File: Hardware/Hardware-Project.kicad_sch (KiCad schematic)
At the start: 2 parts

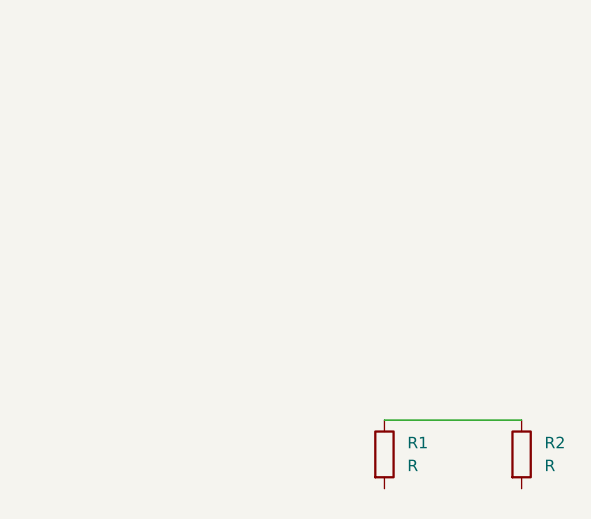
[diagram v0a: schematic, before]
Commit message: Added STM32F446RE symbol and footprint
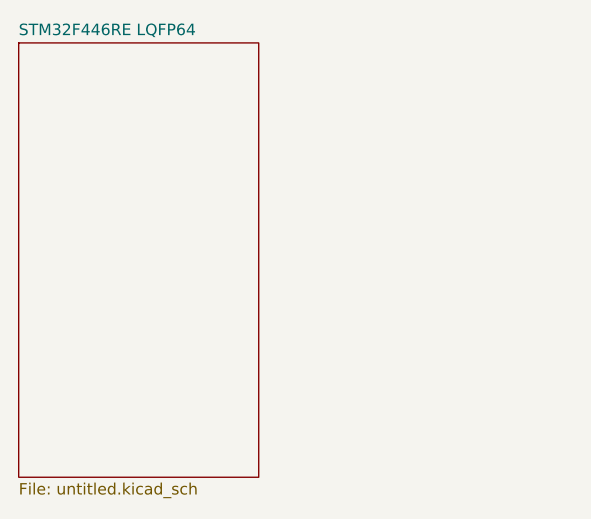
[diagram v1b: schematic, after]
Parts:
- removed R1, R2: R, symbol Device:R
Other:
- added sheet STM32F446RE LQFP64 (untitled.kicad_sch)
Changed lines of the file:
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@@
 	(generator_version "9.0")
 	(paper "A4")
-	(wire
-		(pts
-			(xy 91.44 80.01) (xy 106.68 80.01)
-		)
-		(stroke
-			(width 0)
-			(type default)
-		)
-	)
-	(symbol
-		(lib_id "Device:R")
-		(at 106.68 83.82 0)
-		(unit 1)
+	(sheet
+		(at 50.8 38.1)
+		(size 26.67 48.26)
 		(exclude_from_sim no)
 		(in_bom yes)
@@
 		(dnp no)
 		(fields_autoplaced yes)
-		(property "Reference" "R2"
-			(at 109.22 82.5499 0)
+		(stroke
+			(width 0.1524)
+			(type solid)
+		)
+		(fill
+			(color 0 0 0 0.0000)
+		)
+		(property "Sheetname" "STM32F446RE LQFP64"
+			(at 50.8 37.3884 0)
 			(effects
 				(font
 					(size 1.27 1.27)
 				)
-				(justify left)
+				(justify left bottom)
 			)
 		)
-		(property "Value" "R"
-			(at 109.22 85.0899 0)
+		(property "Sheetfile" "untitled.kicad_sch"
+			(at 50.8 86.9446 0)
 			(effects
 				(font
 					(size 1.27 1.27)
 				)
-				(justify left)
+				(justify left top)
 			)
-		)
-		(property "Footprint" ""
-			(at 104.902 83.82 90)
-			(effects
-				(font
-					(size 1.27 1.27)
-				)
-				(hide yes)
-			)
-		)
-		(property "Datasheet" "~"
-			(at 106.68 83.82 0)
-			(effects
-				(font
-					(size 1.27 1.27)
-				)
-				(hide yes)
-			)
-		)
-		(property "Description" "Resistor"
-			(at 106.68 83.82 0)
-			(effects
-				(font
-					(size 1.27 1.27)
-				)
-				(hide yes)
-			)
-		)
-		(pin "2"
-		)
-		(pin "1"
 		)
 		(instances
 			(project "Hardware-Project"
 				(path "/16e232dd-2018-4914-997b-dd1e00d4fd91"
-					(reference "R2")
-					(unit 1)
+					(page "2")
 				)
 			)
-		)
-	)
-	(symbol
-		(lib_id "Device:R")
-		(at 91.44 83.82 0)
-		(unit 1)
-		(exclude_from_sim no)
-		(in_bom yes)
-		(on_board yes)
-		(dnp no)
-		(fields_autoplaced yes)
-		(property "Reference" "R1"
-			(at 93.98 82.5499 0)
-			(effects
-				(font
-					(size 1.27 1.27)
-				)
-				(justify left)
-			)
-		)
-		(property "Value" "R"
-			(at 93.98 85.0899 0)
-			(effects
-				(font
-					(size 1.27 1.27)
-				)
-				(justify left)
-			)
-		)
-		(property "Footprint" ""
-			(at 89.662 83.82 90)
-			(effects
-				(font
-					(size 1.27 1.27)
-				)
-				(hide yes)
-			)
-		)
-		(property "Datasheet" "~"
-			(at 91.44 83.82 0)
-			(effects
-				(font
-					(size 1.27 1.27)
-				)
-				(hide yes)
-			)
-		)
-		(property "Description" "Resistor"
-			(at 91.44 83.82 0)
-			(effects
-				(font
-					(size 1.27 1.27)
-				)
-				(hide yes)
-			)
-		)
-		(pin "2"
-		)
-		(pin "1"
-		)
-		(instances
-			(project ""
-				(path "/16e232dd-2018-4914-997b-dd1e00d4fd91"
-					(reference "R1")
-					(unit 1)
-				)
-			)

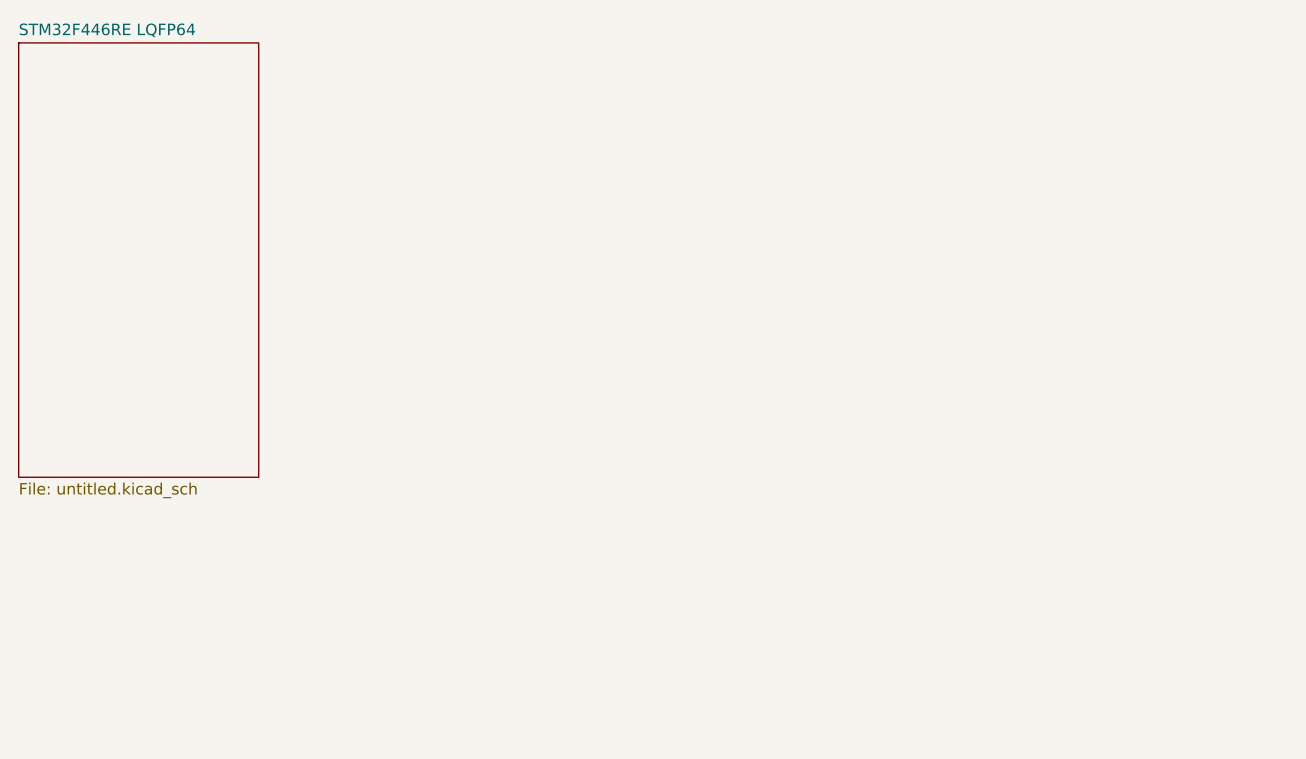
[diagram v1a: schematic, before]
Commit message: Added hierarchal sheets for the IMU and USB connectors. FInalized the design of USB and ESD protection
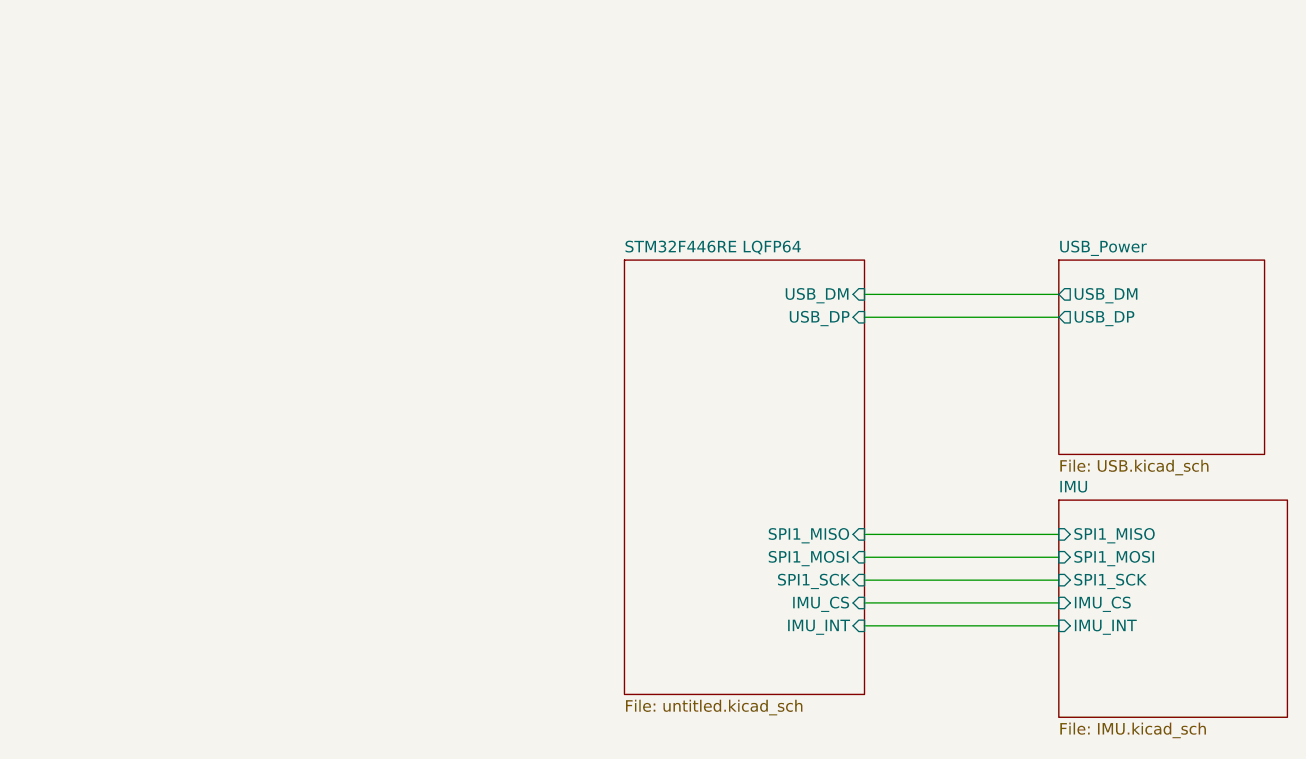
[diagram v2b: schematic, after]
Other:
- added sheet IMU (IMU.kicad_sch)
- added sheet USB_Power (USB.kicad_sch)
- sheet STM32F446RE LQFP64 ports: added IMU_CS, IMU_INT, SPI1_MISO, SPI1_MOSI, SPI1_SCK, USB_DM, USB_DP; removed none

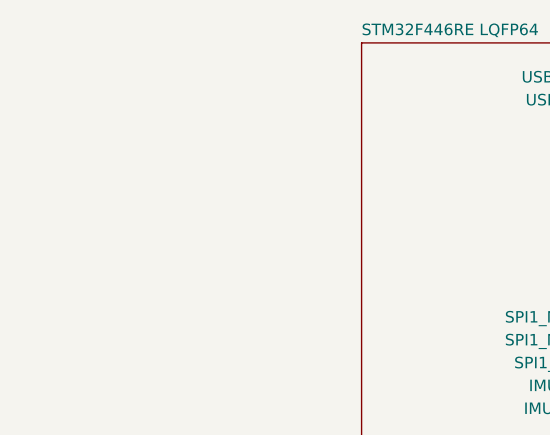
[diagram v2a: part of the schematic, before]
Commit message: Added the SD Card reader component.
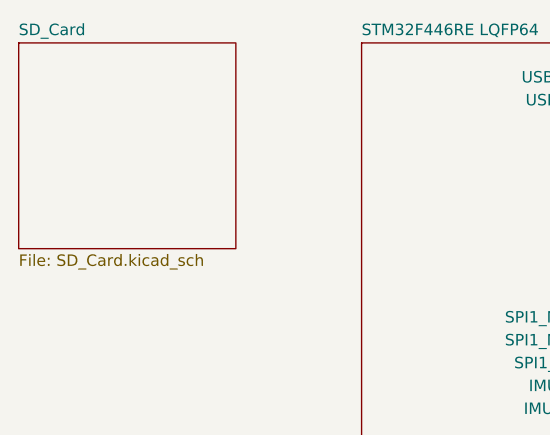
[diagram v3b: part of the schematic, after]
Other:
- added sheet SD_Card (SD_Card.kicad_sch)
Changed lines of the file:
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@@
+	)
+	(sheet
+		(at 80.01 62.23)
+		(size 24.13 22.86)
+		(exclude_from_sim no)
+		(in_bom yes)
+		(on_board yes)
+		(dnp no)
+		(fields_autoplaced yes)
+		(stroke
+			(width 0.1524)
+			(type solid)
+		)
+		(fill
+			(color 0 0 0 0.0000)
+		)
+		(property "Sheetname" "SD_Card"
+			(at 80.01 61.5184 0)
+			(effects
+				(font
+					(size 1.27 1.27)
+				)
+				(justify left bottom)
+			)
+		)
+		(property "Sheetfile" "SD_Card.kicad_sch"
+			(at 80.01 85.6746 0)
+			(effects
+				(font
+					(size 1.27 1.27)
+				)
+				(justify left top)
+			)
+		)
+		(instances
+			(project "Hardware-Project"
+				(path "/16e232dd-2018-4914-997b-dd1e00d4fd91"
+					(page "5")
+				)
+			)
+		)
 	)
 	(sheet

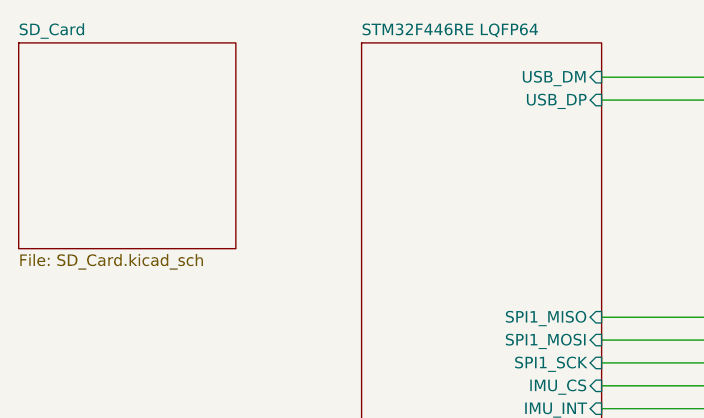
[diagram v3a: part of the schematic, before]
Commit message: Added hierarchal labels to main STM sheet and wired connections to SD card module
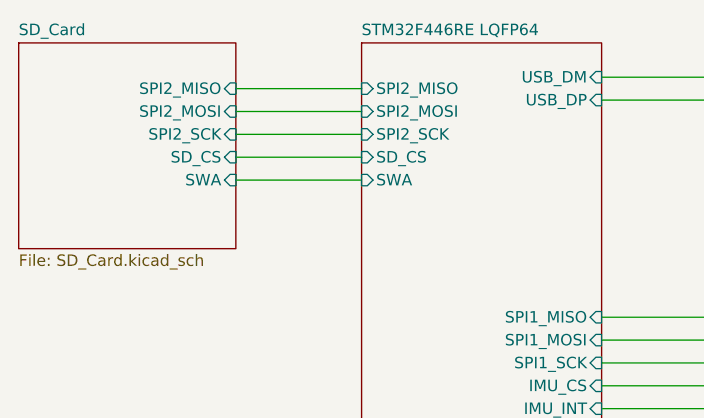
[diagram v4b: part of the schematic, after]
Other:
- sheet SD_Card ports: added SD_CS, SPI2_MISO, SPI2_MOSI, SPI2_SCK, SWA; removed none
- sheet STM32F446RE LQFP64 ports: added SD_CS, SPI2_MISO, SPI2_MOSI, SPI2_SCK, SWA; removed none
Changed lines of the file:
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@@
+	(wire
+		(pts
+			(xy 104.14 74.93) (xy 118.11 74.93)
+		)
+		(stroke
+			(width 0)
+			(type default)
+		)
+	)
+	(wire
+		(pts
+			(xy 104.14 72.39) (xy 118.11 72.39)
+		)
+		(stroke
+			(width 0)
+			(type default)
+		)
+	)
 	(wire
 		(pts
@@
 	(wire
 		(pts
+			(xy 104.14 67.31) (xy 118.11 67.31)
+		)
+		(stroke
+			(width 0)
+			(type default)
+		)
+	)
+	(wire
+		(pts
 			(xy 144.78 100.33) (xy 166.37 100.33)
 		)
@@
 	(wire
 		(pts
+			(xy 104.14 69.85) (xy 118.11 69.85)
+		)
+		(stroke
+			(width 0)
+			(type default)
+		)
+	)
+	(wire
+		(pts
 			(xy 144.78 95.25) (xy 166.37 95.25)
+		)
+		(stroke
+			(width 0)
+			(type default)
+		)
+	)
+	(wire
+		(pts
+			(xy 104.14 77.47) (xy 118.11 77.47)
 		)
 		(stroke
@@
 			)
 		)
+		(pin "SPI2_MISO" input
+			(at 104.14 67.31 0)
+			(effects
+				(font
+					(size 1.27 1.27)
+				)
+				(justify right)
+			)
+		)
+		(pin "SPI2_MOSI" input
+			(at 104.14 69.85 0)
+			(effects
+				(font
+					(size 1.27 1.27)
+				)
+				(justify right)
+			)
+		)
+		(pin "SPI2_SCK" input
+			(at 104.14 72.39 0)
+			(effects
+				(font
+					(size 1.27 1.27)
+				)
+				(justify right)
+			)
+		)
+		(pin "SD_CS" input
+			(at 104.14 74.93 0)
+			(effects
+				(font
+					(size 1.27 1.27)
+				)
+				(justify right)
+			)
+		)
+		(pin "SWA" input
+			(at 104.14 77.47 0)
+			(effects
+				(font
+					(size 1.27 1.27)
+				)
+				(justify right)
+			)
+		)
 		(instances
 			(project "Hardware-Project"
@@
 			)
 		)
+		(pin "SPI2_MISO" input
+			(at 118.11 67.31 180)
+			(effects
+				(font
+					(size 1.27 1.27)
+				)
+				(justify left)
+			)
+		)
+		(pin "SPI2_MOSI" input
+			(at 118.11 69.85 180)
+			(effects
+				(font
+					(size 1.27 1.27)
+				)
+				(justify left)
+			)
+		)
+		(pin "SPI2_SCK" input
+			(at 118.11 72.39 180)
+			(effects
+				(font
+					(size 1.27 1.27)
+				)
+				(justify left)
+			)
+		)
+		(pin "SD_CS" input
+			(at 118.11 74.93 180)
+			(effects
+				(font
+					(size 1.27 1.27)
+				)
+				(justify left)
+			)
+		)
+		(pin "SWA" input
+			(at 118.11 77.47 180)
+			(effects
+				(font
+					(size 1.27 1.27)
+				)
+				(justify left)
+			)
+		)
